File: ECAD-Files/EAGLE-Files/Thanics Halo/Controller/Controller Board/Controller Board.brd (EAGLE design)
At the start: 95.5 x 57.8 mm, 162 parts, among them J10 EDGE_CONNECTOR_20POS, J2 3.5_TOUCHSCREEN, J3 USB_MICRO_B_SMT, J5 EDGE_CONNECTOR_20POS, J6 POWER_CONNECTOR, J7 HDMI, J8 2_PIN_CONNECTOR, J9 USB_A_RECEPT, Q2 2N7002P_MOSFET, U1 AAT3620_BATT_CHARGER, U10 TPS6209, U11 LM3880MF-1AA/NOPBMF06A-M, U12 APPLE_2.0C_COPROCESSOR, U16 MIC23050, U19 WM8960, U2 8 CH, U4 PDDL2450, U7 ESD5384, U8 PEC12R, U9 PEC12R, Y1 DSC6001

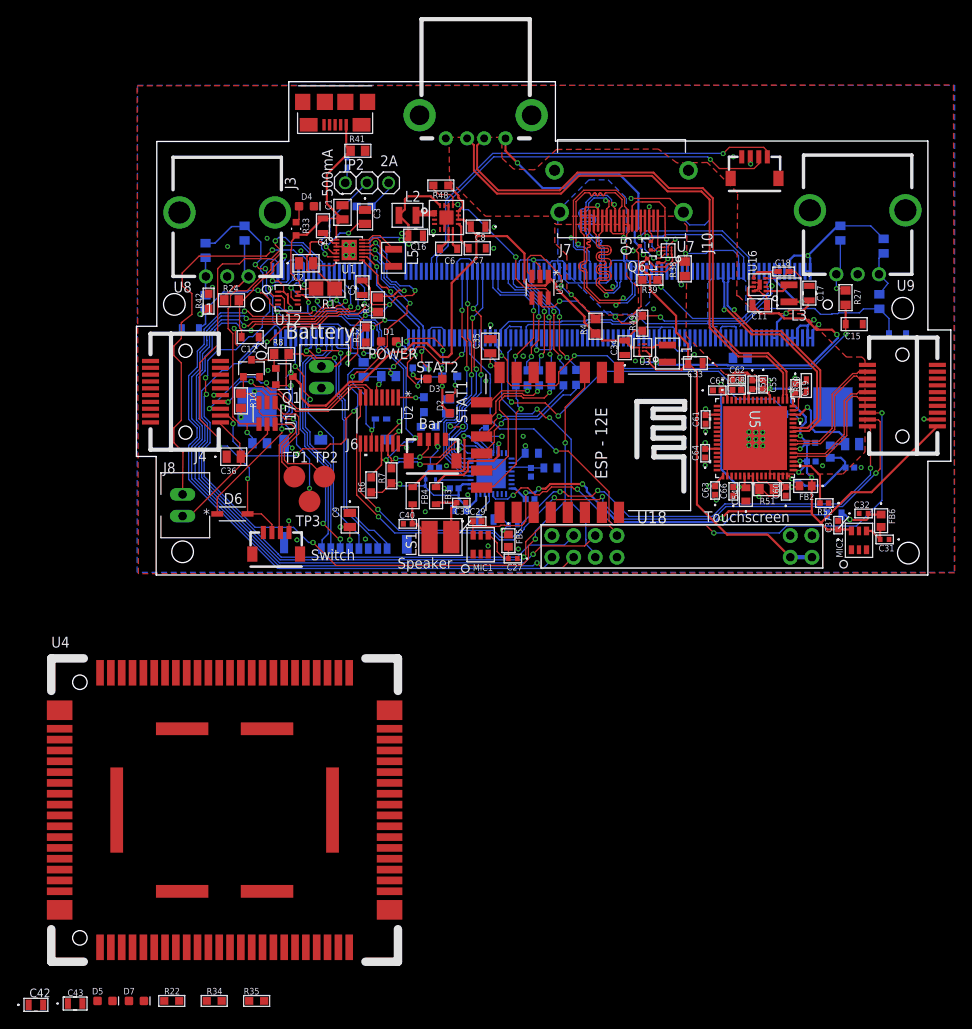
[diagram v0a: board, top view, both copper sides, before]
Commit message: Finished controller board v1.5
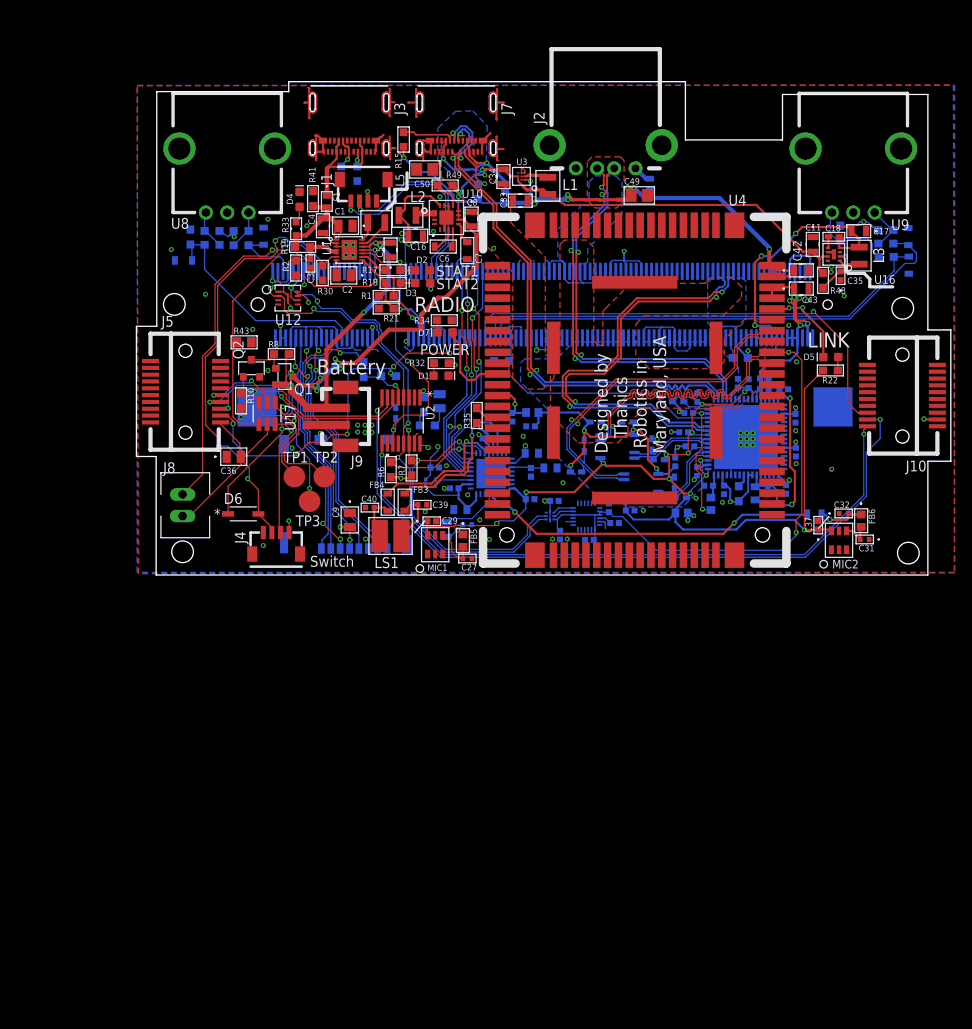
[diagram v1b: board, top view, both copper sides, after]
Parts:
- removed J11: (no value), thanics_robotics:JST_SH_4POS
- removed JP2: (no value), Controller Board:1X03
- removed Q5, Q6: (no value), Controller Board:SOT-523
- removed R31: 20R, Controller Board:RC0603N-M
- removed R38: NF, Controller Board:RC0805N
- removed R39: 100k, Controller Board:RC0603N-M
- removed R4: 10k, Controller Board:RC0805N
- removed U$2: MICROSD, Controller Board:MICROSD
- removed U18: (no value), Controller Board:ESP12E-SMD
- added C44, C45, C46, C47, C51, C52, C56, C69: 0.1uF, 0.1uF-capacitor-0402:0402-M
- added C48: 1uF, thanics-capacitor:C0402
- added C49, C50: 22uF, thanics-capacitor:C0805
- added F1, F2, F3: MFU0603FF01600P100, 1.6a-fuse:FUS_VISHAY_MFU0603
- added L4: 1k@100MHz, 600ohm-fb:IND_BLM18_0603-M
- added R36, R37, R44, R46, R47, R53, R54, R55: 49R9, 49.9-resistor:RC0402N-M
- added T1, T2: ALT4532M, thanics_robotics:ALT4532
- C3: value 1uF -> 1uF; device Controller Board:YAG_CC0805 -> thanics-capacitor:C0402
- C35: device Controller Board:0805 -> 0.1uF-capacitor-0402:0402-M
- C53: value 1uF -> 0.1uF; device 1uF X7R Ceramic Capacitor:YAG_CC0805 -> 0.1uF-capacitor-0402:0402-M
- J2: value 3.5_TOUCHSCREEN -> USB_A_RECEPT; device Controller Board:3.5_TOUCHSCREEN -> Controller Board:USB_A_RECEPT
- J3: value USB_MICRO_B_SMT -> 105450-0101; device Controller Board:USB_MICRO_B_SMT -> 105450-0101:MOLEX_105450-0101
- J6: value POWER_CONNECTOR -> MICROSD; device Controller Board:XH_CONNECTOR -> Controller Board:MICROSD
- J7: value HDMI -> 105450-0101; device Controller Board:HDMI -> 105450-0101:MOLEX_105450-0101
- J9: value USB_A_RECEPT -> B2B-PH-SM4-TB(LF)(SN); device Controller Board:USB_A_RECEPT -> thanics-connector:B2B-PH-SM4-TB(LF)(SN)
- R1: value 100 -> 10k; device Controller Board:1206 -> 10k-resistor(0603):RC0603N-M
- R10, R16, R2, R23, R24, R25, R26, R27, R28, R29, R41, R45, R5, R8, R9: device Controller Board:RC0805N -> 10k-resistor(0603):RC0603N-M
- R11, R15: value 20R -> 22k; device Controller Board:RC0603N-M -> thanics-resistor:R0603
- R14: value 20R -> 5.1k; device Controller Board:RC0603N-M -> thanics-resistor:R0603
- R17: value 20R -> 1k; device Controller Board:RC0603N-M -> 1k-resistor:RC0603N-M
- R18: value 340R -> 1k; device Controller Board:RC0603N -> 1k-resistor:RC0603N-M
- R19: value 24.9k -> 100R; device Controller Board:RC0402N-M -> 100-resistor:RC0603N-M
- R21: value 20R -> 10k; device Controller Board:RC0603N-M -> 10k-resistor(0603):RC0603N-M
- R3: value 100k -> 5.1k; device Controller Board:RC0603N-M -> thanics-resistor:R0603
- R30: value 20R -> 75k; device Controller Board:RC0603N-M -> thanics-resistor:R0603
- R51: device 10k-resistor:RC0805N -> 10k-resistor(0603):RC0603N-M
- U11: value LM3880MF-1AA/NOPBMF06A-M -> (none); device Controller Board:MF06A-M -> ICM-20948-mpu:QFN40P300X300X105-25N
- U7: value ESD5384 -> (none); device Controller Board:WLCSP9 -> thanics_robotics:8-UMLP
- moved C42 124.4 mm to (79.8, 35.8)
- moved C43 119.5 mm to (79.8, 33.6)
- moved D5 113.7 mm to (83.3, 25.6), turned to 180 degrees
- moved R22 106.9 mm to (83.2, 24.0), turned to 180 degrees
- moved D7 86.3 mm to (38.0, 28.5), turned to 180 degrees
- moved R34 84.2 mm to (37.9, 29.9)
- moved R35 73.3 mm to (41.8, 18.7), turned to 90 degrees
- moved U4 68.8 mm to (60.3, 21.7), turned to 90 degrees
- moved R48 46.2 mm to (82.3, 34.6), turned to 90 degrees
- moved J1 46.1 mm to (28.5, 43.9), turned to 0 degrees
- moved J2 45.8 mm to (56.9, 47.7)
- moved C35 41.9 mm to (84.4, 35.1), turned to 90 degrees
- moved J9 37.0 mm to (24.1, 18.6), turned to 270 degrees
- moved U7 34.1 mm to (50.3, 6.96), flipped to the bottom, turned to 90 degrees
- moved R15 33.6 mm to (33.2, 51.1), flipped to the top, turned to 270 degrees
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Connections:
- removed net EMMC_EN_N_1V8: U6.90
- removed net HDMI_HPD_N_1V8: Q5.D, R39.2, U6.88
- removed net IRQ: J2.4, U6.70
- removed net N$25: R15.1, U18.GPIO9
- removed net N$26: R21.1, U18.GPIO10
- removed net N$27: R30.1, U18.MOSI
- removed net N$40: JP2.1, R3.2
- removed net N$42: JP2.3, R19.2
- removed net N$8: R48.2, U10.13, U11.6
- removed net POWER_SEQ_EN: R4.2, U11.3
- new net I2C_SCL_1V8: U11.23, U7.7
- new net I2C_SDA_1V8: U11.24, U7.6
- new net N$47: F1.1, J3.A4, J3.A9, J3.B4, J3.B9
- new net N$51: C50.1, F2.1, J7.A4, J7.A9, J7.B4, J7.B9
- new net N$63: J7.B5, R15.1
- new net N$70: C45.2, C46.2, L4.1, R47.1, R53.1, R54.1, R55.1, T1.6, T2.6
- new net N$71: F3.2, J2.1
- net +1V8: now also C51.1, C52.2, C69.1, U11.13, U11.22, U11.8, U11.9, U7.8; no longer R39.1
- net +3V3: now also C56.2, J6.4, U7.1, U7.5; no longer C35.2, J11.2, R38.1, U$2.4, U18.VCC
- net +5V: now also C49.1, F2.2, F3.1, R11.2, R15.2; no longer J2.1, J2.2, J9.1, Q6.G, U7.A1, U7.B1, U7.C1
- net 3.3V_A: now also C47.2, R36.1, R37.1, R44.1, R46.1, T1.3, T2.3; no longer J10.1
- net BATT_OUTPUT: now also R48.2; no longer R4.1, R48.1, U11.1
- net ETH_BIAS: now also C44.2, L4.2
- net GND: now also C3.2, C44.1, C45.1, C46.1, C47.1, C48.2, C49.2, C50.2, C51.2, C52.1, C56.1, C69.2, J2.4, J2.5, J2.6, J3.1, J3.2, J3.3, J3.A1, J3.A12, J3.B1, J3.B12, J6.10, J6.11, J6.12, J6.13, J6.6, J6.9, J7.1, J7.3, J7.4, J7.A1, J7.A12, J7.B1, J7.B12, J9.2, R1.2, R14.1, R21.2, R30.1, U11.11, U11.18, U11.20, U7.4; no longer C3.1, J11.1, J2.3, J2.7, J3.5, J3.6, J3.7, J3.P$1, J3.P$2, J3.P$3, J3.P$4, J6.2, J7.11, J7.17, J7.5, J7.8, J7.P$1, J7.P$2, J7.P$3, J7.P$4, J9.4, J9.5, J9.6, Q5.S, R19.1, U$2.10, U$2.11, U$2.12, U$2.13, U$2.6, U$2.9, U11.2, U18.GND, U7.B2, U7.C2
- net HDMI_CEC: no longer Q6.S, R38.2
- net HDMI_CK_N: no longer J7.12
- net HDMI_CK_P: no longer J7.10
- net HDMI_D0_N: no longer J7.9
- net HDMI_D0_P: no longer J7.7
- net HDMI_D1_N: no longer J7.6
- net HDMI_D1_P: no longer J7.4
- net HDMI_D2_N: no longer J7.3
- net HDMI_D2_P: no longer J7.1
- net HDMI_SCL: no longer J7.15, U7.A3
- net HDMI_SDA: no longer J7.16, U7.B3
- net I2C_SCL: now also U7.2; no longer J11.4
- net I2C_SDA: now also U7.3; no longer J11.3
- net ID_SD: no longer U18.CH_PD
- net ISET: now also R30.2; no longer JP2.2
- net J2_SW: now also U6.72; no longer U6.66
- net N$12: now also C35.2, R48.1; no longer R49.2, U11.5
- net N$3: now also R49.2, U10.13; no longer R14.1, U18.MISO
- net N$46: now also J3.B5, R14.2; no longer R31.1, U18.SCLK
- net N$49: now also J3.A5, R3.2; no longer J7.13, Q6.D, U7.A2
- net N$50: now also J7.A5, R11.1; no longer J7.19, Q5.G, U7.C3
- net N$59: now also C48.1; no longer C53.2
- net N$6: now also C3.1, R19.2; no longer C3.2, R1.1
- net N$7: now also C53.2, U11.10; no longer R11.1, U18.CS0
- net RX_LAN_N: now also R54.2, T1.1
- net RX_LAN_P: now also R53.2, T1.2
- net RX_N: now also R46.2, T1.5; no longer J10.15
- net RX_P: now also R44.2, T1.4; no longer J10.16
- net SDX_CLK: now also J6.5; no longer U$2.5
- net SDX_CMD: now also J6.3; no longer U$2.3
- net SDX_D0: now also J6.7; no longer U$2.7
- net SDX_D1: now also J6.8; no longer U$2.8
- net SDX_D2: now also J6.1; no longer U$2.1
- net SDX_D3: now also J6.2; no longer U$2.2
- net SD_CLK: no longer R31.2
- net SD_CMD: no longer R11.2
- net SD_D0: no longer R14.2
- net SD_D1: no longer R30.2
- net SD_D2: no longer R15.2
- net SD_D3: no longer R21.2
- net SPI_CS0: no longer J2.5
- net SPI_CS1: no longer J2.6
- net SPI_MISO: no longer J2.9
- net SPI_MOSI: no longer J2.10
- net SPI_SCLK: no longer J2.8
- net STAT1: now also R1.1
- net STAT2: now also R21.1
- net SWITCH_IN: now also J9.1; no longer J6.1
- net TX_LAN_N: now also R47.2, T2.1
- net TX_LAN_P: now also R55.2, T2.2
- net TX_N: now also R37.2, T2.5; no longer J10.12
- net TX_P: now also R36.2, T2.4; no longer J10.13
- net USB_5V: now also F1.2, R19.1; no longer J3.1, R1.2
- net USB_D2_N: now also J7.A7, J7.B7; no longer J9.2
- net USB_D2_P: now also J7.A6, J7.B6; no longer J9.3
- net USB_D3_N: now also J2.2
- net USB_D3_P: now also J2.3
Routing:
- net ID_SD: track 101.4 -> 0.00 mm, vias 5 -> 0
- net SPI_MOSI: track 98.2 -> 0.00 mm, vias 3 -> 0
- net SPI_MISO: track 93.7 -> 0.00 mm, vias 3 -> 0
- net SPI_CS0: track 90.6 -> 0.00 mm, vias 3 -> 0
- net SPI_CS1: track 87.1 -> 0.00 mm, vias 2 -> 0
- net SPI_SCLK: track 87.0 -> 0.00 mm, vias 2 -> 0
- net +1V8: track 43.3 -> 94.8 mm, vias 3 -> 5
- net USB_D3_N: track 0.00 -> 46.3 mm, vias 0 -> 3
- net USB_D3_P: track 0.00 -> 46.0 mm, vias 0 -> 3
- net +3V3: track 208.0 -> 165.6 mm, vias 34 -> 33
- net RX_LAN_P: track 0.00 -> 42.2 mm, vias 0 -> 1
- net RX_LAN_N: track 0.00 -> 41.8 mm, vias 0 -> 1
- net TX_LAN_P: track 0.00 -> 35.5 mm, vias 0 -> 1
- net TX_LAN_N: track 0.00 -> 35.5 mm, vias 0 -> 1
- net IRQ: track 33.8 -> 0.00 mm, vias 2 -> 0
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- added copper zone on layer 1, net N$25
- added copper zone on layer 1, net N$26
- added copper zone on layer 16, net N$27
- added copper zone on layer 16, net N$40
- added copper zone on layer 16, net N$42
- added copper zone on layer 1, net N$8
- added copper zone on layer 1, net USB_5V
- removed copper zone on layer 1, net N$47
- removed copper zone on layer 1, net N$51
- removed copper zone on layer 16, net N$63
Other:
- outline, holes or cut-outs redrawn
- board text added: "Controller Board v1.5"
- board text added: "LINK"
- board text added: "MIC2"
- board text added: "RADIO"
- board text added: "U10"
- board text removed: "2A"
- board text removed: "500mA"
- board text removed: "Bar"
- board text removed: "Controller Board v4"
- board text removed: "J1"
- board text removed: "J10"
- board text removed: "J3"
- board text removed: "J4"
- board text removed: "J6"
- board text removed: "J7"
- board text removed: "JP2"
- board text removed: "Q5"
- board text removed: "Q6"
- board text removed: "Speaker"
- board text removed: "Touchscreen"
- board text removed: "U7"

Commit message: Added new battery and joystick modules
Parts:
- removed C33: 10uF, Controller Board:G-21
- removed U3: (no value), Controller Board:YFF9
- added C70: 22uF, Controller Board:G-21
- added R31, R4: 10k, 10k-resistor(0603):RC0603N-M
- added U13: MIC2876UDFN-8, thanics_robotics:UDFN8
- moved L1 0.10 mm to (50.2, 45.7), turned to 90 degrees
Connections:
- net +3V3: now also J10.11; no longer J10.2
- net +5V: now also C70.2, U13.5, U13.8; no longer C33.2, U3.A1, U3.A2
- net BATT_OUTPUT: now also U13.3, U13.6; no longer U3.A3, U3.B3
- net GND: now also C70.1, J10.15, R31.2, R4.2, U13.2, U13.4, U13.EP; no longer C33.1, J10.11, J10.14, J10.17, U3.C1, U3.C2
- net J1_SW: now also R4.1
- net J2_SW: now also J10.12, R31.1; no longer J10.18
- net N$19: now also J10.13; no longer J10.19
- net N$20: now also J10.14; no longer J10.20
- net N$61: now also U13.1; no longer U3.B1, U3.B2
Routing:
- net BATT_OUTPUT: track 121.0 -> 133.9 mm
- net N$20: track 76.7 -> 83.0 mm
- net +3V3: track 165.6 -> 160.9 mm, vias 33 -> 34
- net N$19: track 86.1 -> 90.7 mm
- net +5V: track 71.2 -> 74.2 mm
- net GND: track 196.4 -> 199.1 mm, vias 71 -> 74
- net J1_SW: track 42.6 -> 44.0 mm
- net J2_SW: track 56.2 -> 54.9 mm
- net N$61: track 3.25 -> 2.27 mm
- added copper zone on layer 1, net +5V
- removed copper zone on layer 2, net N$64
- removed copper zone on layer 15, net N$65
